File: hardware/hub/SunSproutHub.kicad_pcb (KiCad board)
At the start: 6 copper layers, 56 x 85 mm, 141 parts, among them CN5 1755736, J2 Conn_01x02, J201 RJHSE5380, J202 RJHSE5380, J203 Qwiic, J302 JST_PA_S02B-PASK-2, J4 BATTERY, J401 JST_PA_S02B-PASK-2, J6 Qwiic, J7 GPIO_HEADER_L, J8 GPIO_HEADER_R, Q1 MDD3415, Q2 DMP3098L-7, Q3 AO3400A, Q301 AO3400A, Q302 AO3400A, Q303 AO3400A, Q304 AO3400A, SW1 SW_Push, SW2 SW_Push, SW3 SW_Push, U1 ESP32-C5-WROOM-1U, U201 PCA9615, U3 BQ34Z100PWR-G1, U4 TPS631000, U5 TPS22918DBVR, U8 BQ25798RQMR

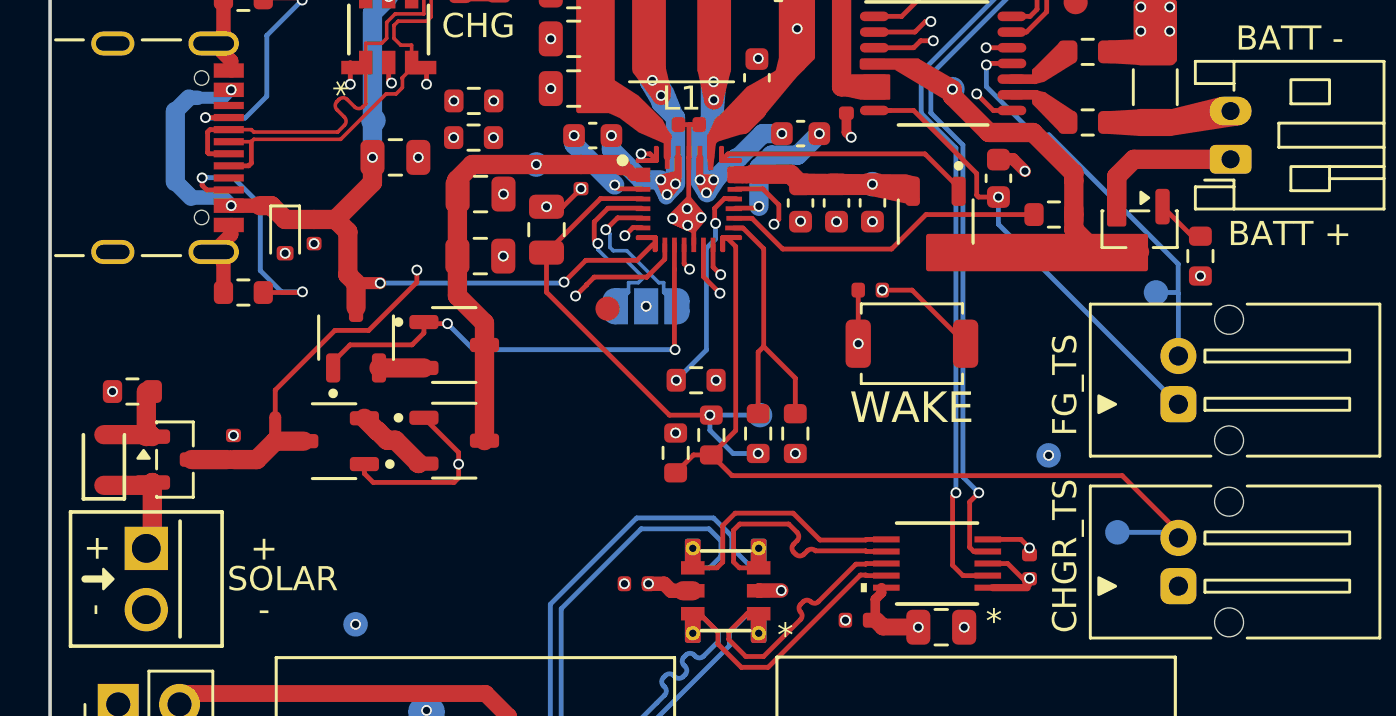
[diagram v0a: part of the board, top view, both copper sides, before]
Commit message: fix(hub): turn reverse-polarity FETs Q1/Q2 around so their body diodes block
Q1 and Q2 had their source on the connector and drain on the board. The
gate turned the channel off on a reversed input, but the body diode then
conducted from the board to the connector and dragged VDC / VBAT_PROTECTED
to roughly the reversed voltage, beyond the charger's -2 V VAC/VBUS rating.

- Swap drain and source on Q1 and Q2: drain on J4 / CN5, source on the
  board.
- Move D2's cathode to VDC so it still clamps Q2 gate-to-source.
- Rewrite the topology section of input-protection.md, and update the
  overview and testing-status pages.

Co-Authored-By: Claude Opus 5.5 <noreply@anthropic.com>
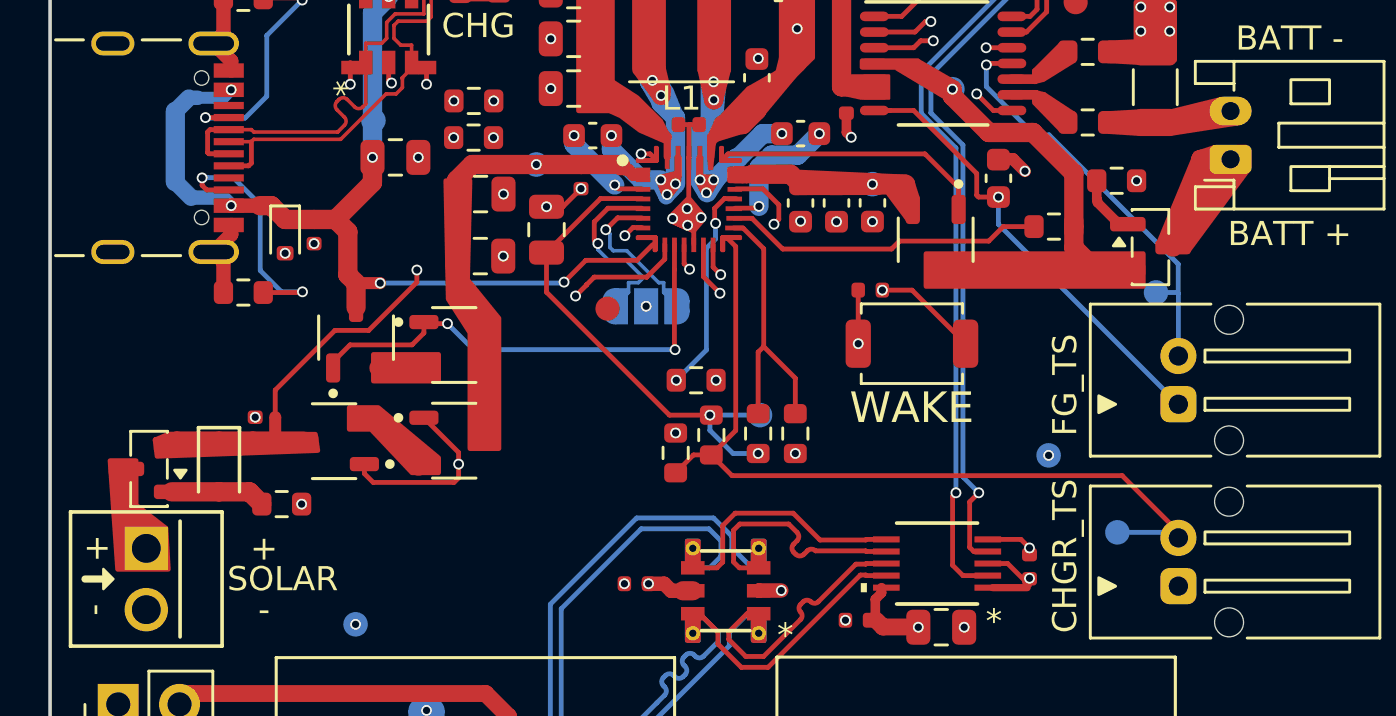
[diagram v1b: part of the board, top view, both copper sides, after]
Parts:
- moved R19 7.75 mm to (34.6, 87.4), turned to 0 degrees
- moved D2 4.78 mm to (32.0, 85.8), turned to -90 degrees
- moved R17 4.67 mm to (69.2, 74.0), turned to 0 degrees
- moved C28 1.17 mm to (33.5, 84.3)
- moved Q2 1.14 mm to (29.1, 85.9), turned to 180 degrees
- moved Q1 0.87 mm to (70.6, 76.8), turned to 0 degrees
- moved Q3 0.75 mm to (61.7, 76.4)
- moved R304 0.50 mm to (66.6, 75.9)
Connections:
- CN5 pad 1: Net-(Q2-S) -> Net-(Q2-D)
- D2 pad 1: Net-(Q2-S) -> VDC
- Q1 pad 2: /VBAT_RAW -> VBAT_PROTECTED
- Q1 pad 3: VBAT_PROTECTED -> /VBAT_RAW
- Q2 pad 2: Net-(Q2-S) -> VDC
- Q2 pad 3: VDC -> Net-(Q2-D)
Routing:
- net Net-(Q2-S): track 4.54 -> 0.00 mm
- net Net-(Q2-D): track 0.00 -> 3.63 mm
- net /VBAT_RAW: track 6.26 -> 5.35 mm
- net SDRV_NODE: track 10.5 -> 11.4 mm
- net VDC: track 4.72 -> 5.56 mm
